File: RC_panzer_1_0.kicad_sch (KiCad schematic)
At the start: 12 parts, among them J1 Conn_01x19_Socket, J10 StepDown_OUT, J2 Conn_01x19_Socket, J3 Motortreiber_links, J4 Motortreiber_rechts, J5 Stepper_driver_links, J6 Stepper_driver_rechts, J7 Screw_Terminal_01x02, J8 Stepper_Ausgang, J9 StepDown_IN

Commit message: tesn
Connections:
- net Quelle- (Masse Quelle) is gone; now on net GND: C2.2, J6.7 (Pin_7), J7.1 (Pin_1), J9.1 (Pin_1)

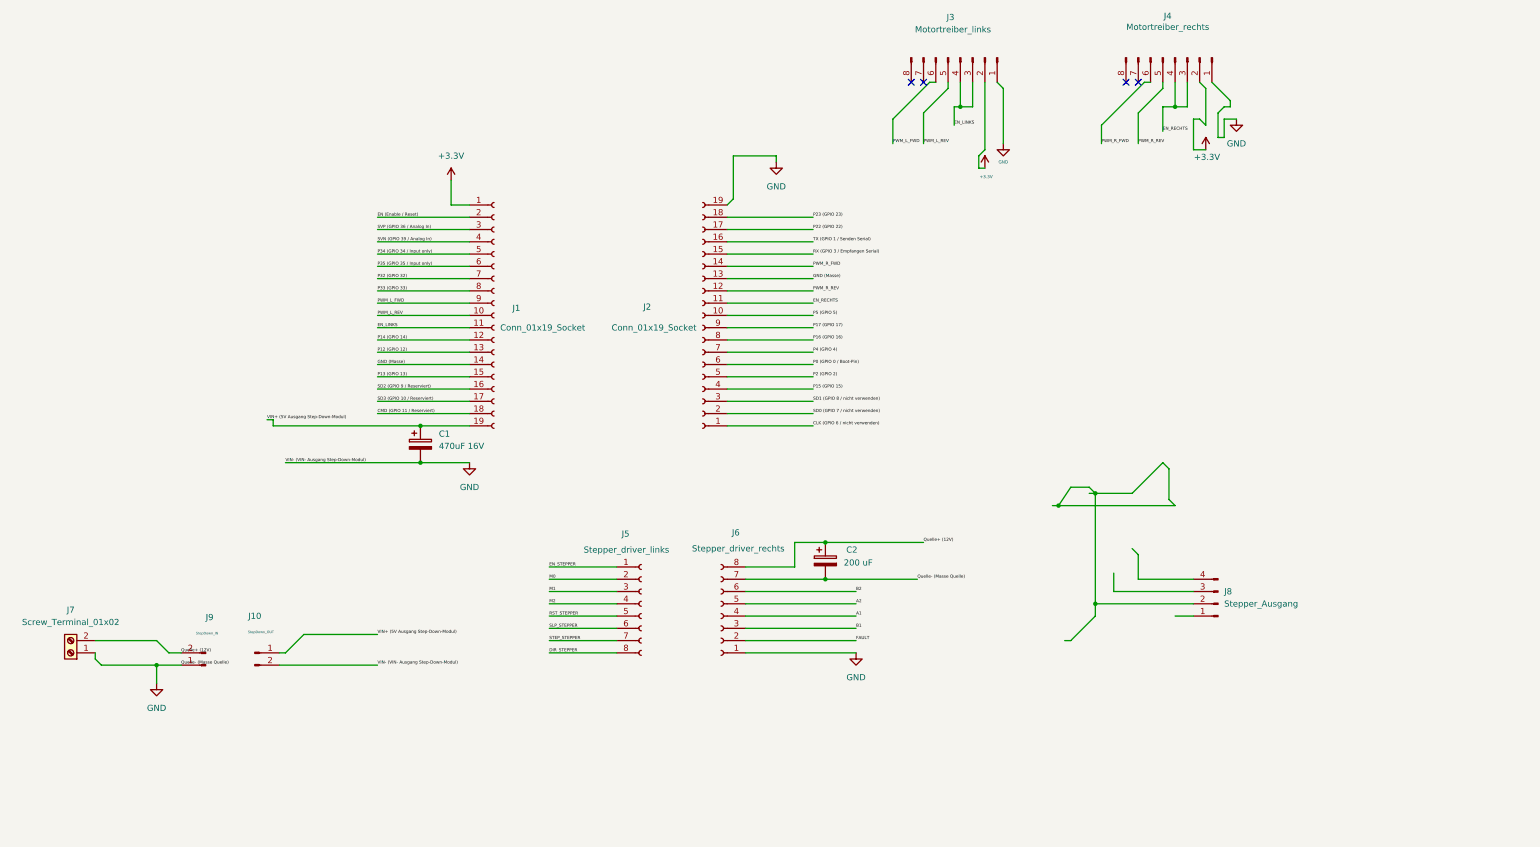
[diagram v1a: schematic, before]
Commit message: Installing the stepper driver
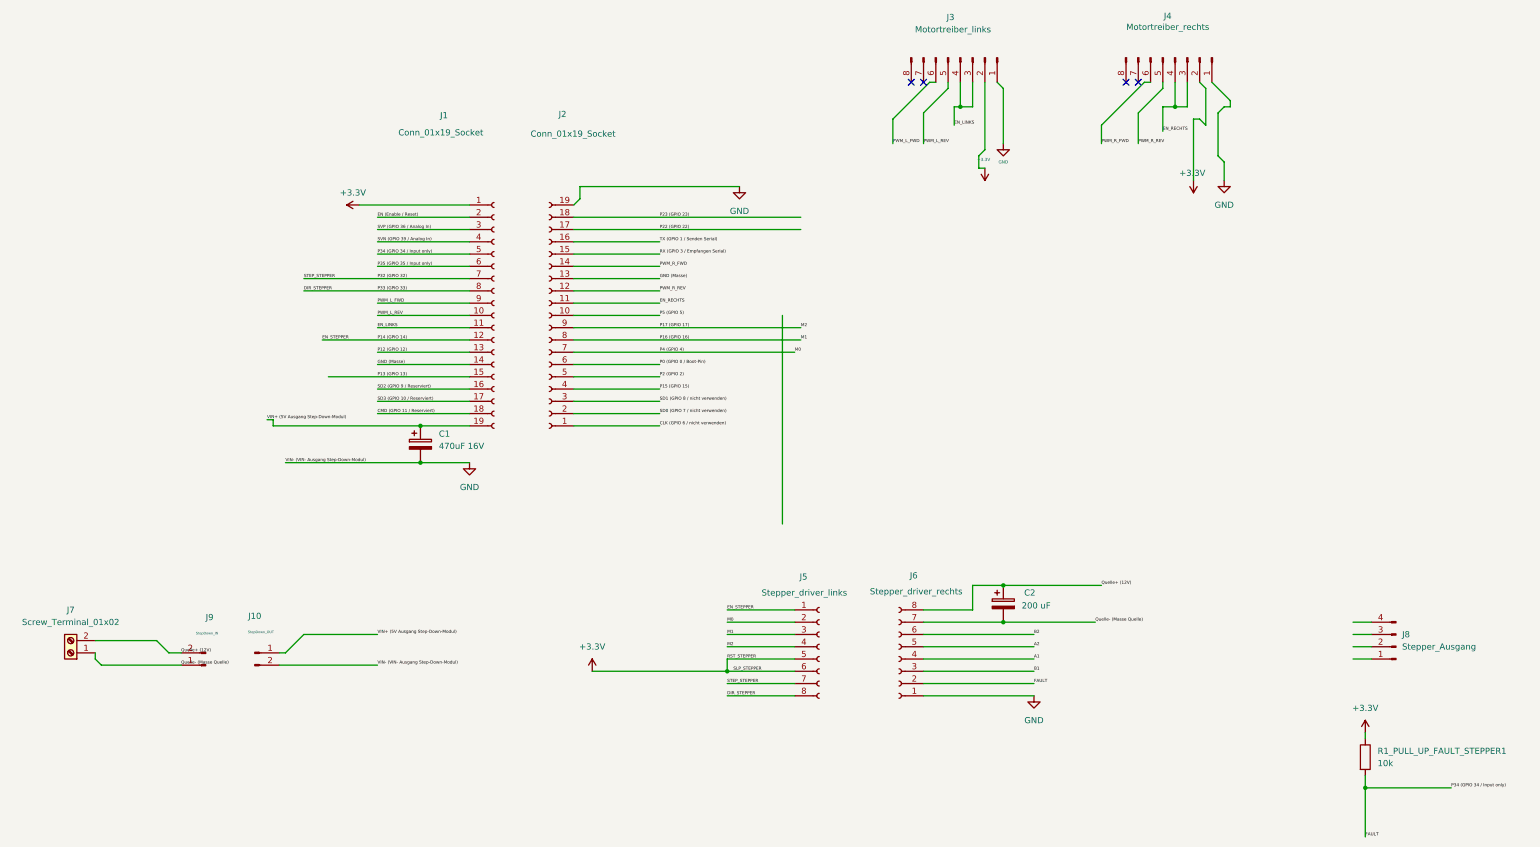
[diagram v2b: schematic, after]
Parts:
- added R1_PULL_UP_FAULT_STEPPER1: 10k, Resistor_THT:R_Axial_DIN0207_L6.3mm_D2.5mm_P10.16mm_Horizontal, symbol Device:R
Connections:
- net P14 (GPIO 14) is gone; now on net EN_STEPPER: J1.12 (Pin_12)
- net P16 (GPIO 16) is gone; now on net M1: J2.8 (Pin_8)
- net P17 (GPIO 17) is gone; now on net M2: J2.9 (Pin_9)
- net P33 (GPIO 33) is gone; now on net DIR_STEPPER: J1.8 (Pin_8)
- net P34 (GPIO 34 / Input only) is gone; now on net FAULT: J1.5 (Pin_5)
- net P4 (GPIO 4) is gone; now on net M0: J2.7 (Pin_7)
- net RST_STEPPER is gone; now on net +3.3V: J5.5 (Pin_5)
- net SLP_STEPPER is gone; now on net +3.3V: J5.6 (Pin_6)
- net STEP_STEPPER is gone; now on net P32 (GPIO 32): J5.7 (Pin_7)
- net +3.3V: now also R1_PULL_UP_FAULT_STEPPER1.1
- net FAULT: now also R1_PULL_UP_FAULT_STEPPER1.2
- net GND: no longer C2.2, J6.7 (Pin_7), J7.1 (Pin_1), J9.1 (Pin_1)
- new net Quelle- (Masse Quelle): C2.2, J6.7 (Pin_7), J7.1 (Pin_1), J9.1 (Pin_1)
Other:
- moved on the sheet: C2, J2, J5, J6, J8
